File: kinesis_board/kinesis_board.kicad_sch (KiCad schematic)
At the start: 18 parts, among them J2 Conn_01x20, J3 Conn_01x20, J4 Conn_02x03_Odd_Even, J5 Screw_Terminal_01x02, J6 Conn_01x07, U1 ATmega16-16A, U2 D1213A-04S, Y1 Crystal

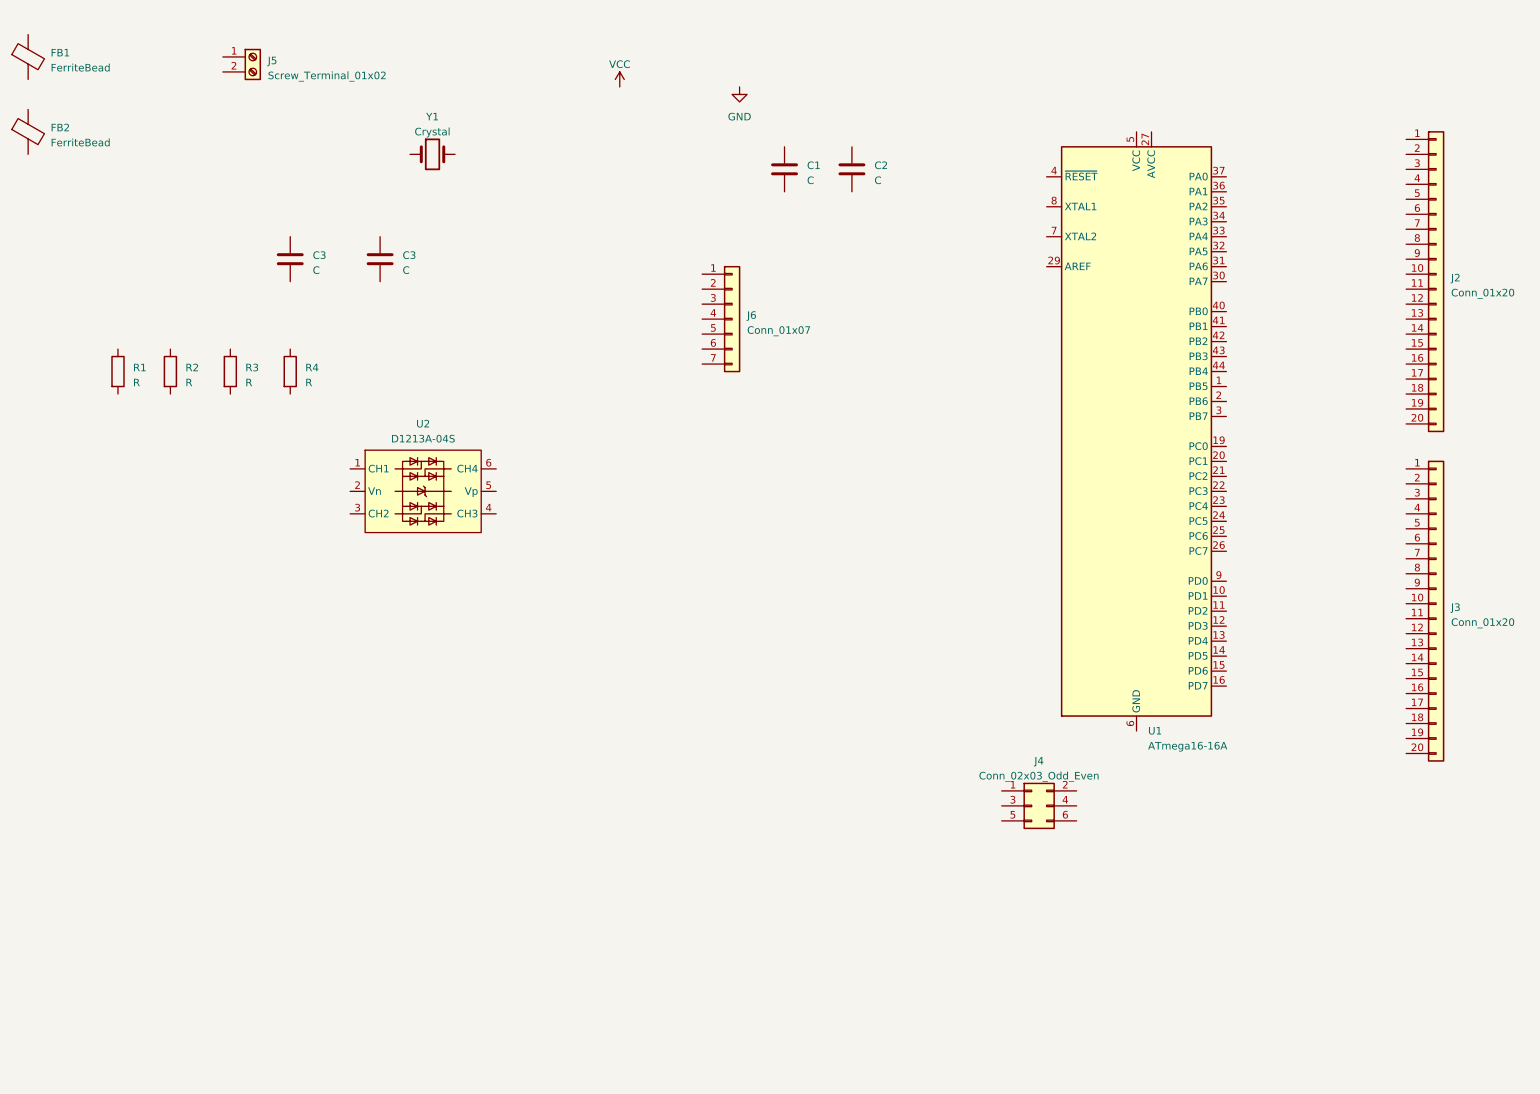
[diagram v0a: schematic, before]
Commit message: finished drawing of the schematics -- needs to be checked before pcb drawing
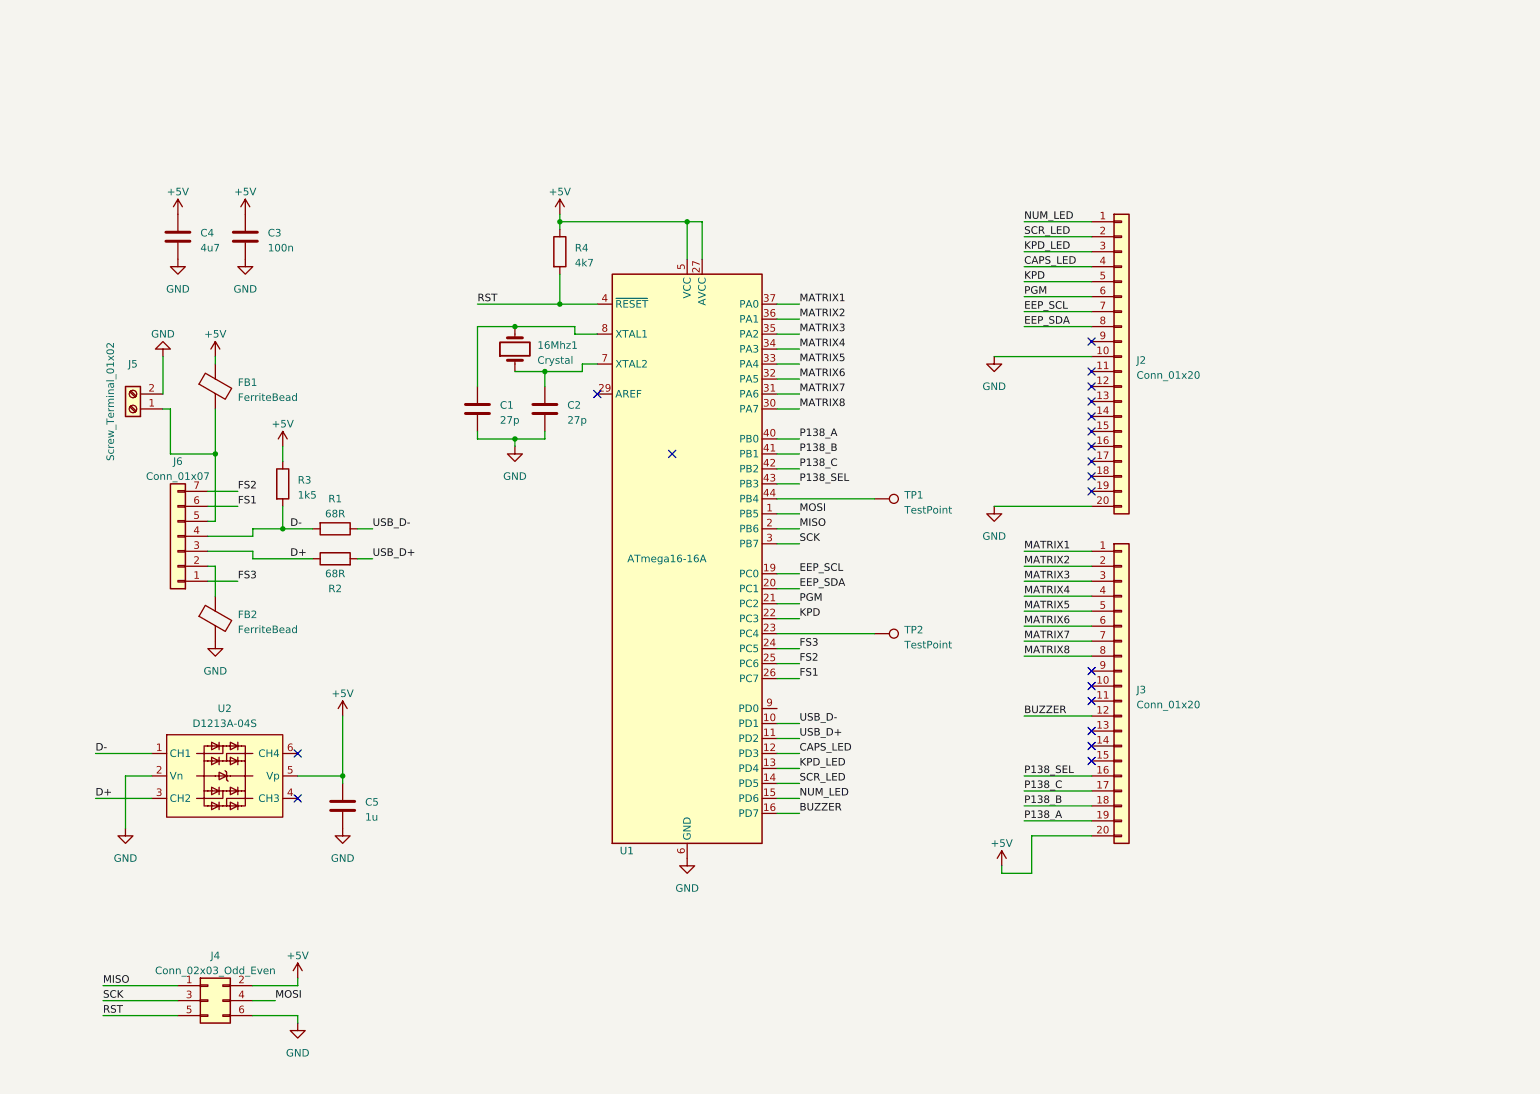
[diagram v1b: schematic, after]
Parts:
- added C5: 1u, Connector_JST:JST_PH_S7B-PH-K_1x07_P2.00mm_Horizontal, symbol Device:C
- added TP1, TP2: TestPoint, TestPoint:TestPoint_Pad_2.0x2.0mm, symbol Connector:TestPoint
- 16Mhz1: renamed from Y1; footprint (none) -> Crystal:Crystal_SMD_HC49-SD_HandSoldering
- C1: value C -> 27p; footprint (none) -> Connector_JST:JST_PH_S7B-PH-K_1x07_P2.00mm_Horizontal
- C2: value C -> 27p; footprint (none) -> Capacitor_SMD:C_0805_2012Metric_Pad1.18x1.45mm_HandSolder
- C3: value C -> 100n; footprint (none) -> Capacitor_SMD:C_0805_2012Metric_Pad1.18x1.45mm_HandSolder
- C4: renamed from C3; value C -> 4u7; footprint (none) -> Capacitor_SMD:C_0805_2012Metric_Pad1.18x1.45mm_HandSolder
- FB1, FB2: footprint (none) -> Inductor_SMD:L_0603_1608Metric_Pad1.05x0.95mm_HandSolder
- J2, J3: footprint (none) -> Connector_PinHeader_2.54mm:PinHeader_1x20_P2.54mm_Vertical_SMD_Pin1Left
- J4: footprint (none) -> Connector_IDC:IDC-Header_2x03_P2.54mm_Horizontal
- J5: footprint (none) -> TerminalBlock_Phoenix:TerminalBlock_Phoenix_MPT-0,5-2-2.54_1x02_P2.54mm_Horizontal
- J6: footprint (none) -> Connector_JST:JST_PH_S7B-PH-K_1x07_P2.00mm_Horizontal
- R1, R2: value R -> 68R; footprint (none) -> Resistor_SMD:R_0805_2012Metric_Pad1.20x1.40mm_HandSolder
- R3: value R -> 1k5; footprint (none) -> Resistor_SMD:R_0805_2012Metric_Pad1.20x1.40mm_HandSolder
- R4: value R -> 4k7; footprint (none) -> Resistor_SMD:R_0805_2012Metric_Pad1.20x1.40mm_HandSolder
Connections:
- net GND: now also C1.2, C2.1, C3.2, C4.2, FB2.2, J2.10 (Pin_10), J2.20 (Pin_20), J4.6 (Pin_6), J5.2 (Pin_2), U1.18 (GND), U1.28 (GND), U1.39 (GND), U1.6 (GND), U2.2 (Vn), C5.2
- net USB_D-: now reaches R1.1
- net USB_D-: now also U1.10 (PD1)
- net D-: now reaches R1.2
- net D-: now also J6.4 (Pin_4), R3.2, U2.1 (CH1)
- net D+: now reaches R2.1
- net D+: now also J6.3 (Pin_3), U2.3 (CH2)
- net USB_D+: now reaches R2.2
- net USB_D+: now also U1.11 (PD2)
- net at J5.1 (Pin_1): now also FB1.2, J6.5 (Pin_5)
- net MATRIX1: now reaches J3.1 (Pin_1)
- net MATRIX1: now also U1.37 (PA0)
- net BUZZER: now reaches J3.12 (Pin_12)
- net BUZZER: now also U1.16 (PD7)
- net P138_SEL: now reaches J3.16 (Pin_16)
- net P138_SEL: now also U1.43 (PB3)
- net P138_C: now reaches J3.17 (Pin_17)
- net P138_C: now also U1.42 (PB2)
- net P138_B: now reaches J3.18 (Pin_18)
- net P138_B: now also U1.41 (PB1)
- net P138_A: now reaches J3.19 (Pin_19)
- net P138_A: now also U1.40 (PB0)
- net MATRIX2: now reaches J3.2 (Pin_2)
- net MATRIX2: now also U1.36 (PA1)
- net +5V: now reaches J3.20 (Pin_20)
- net +5V: now also C3.1, C4.1, FB1.1, J4.2 (Pin_2), R3.1, R4.1, U1.17 (VCC), U1.27 (AVCC), U1.38 (VCC), U1.5 (VCC), U2.5 (Vp), C5.1
- net MATRIX3: now reaches J3.3 (Pin_3)
- net MATRIX3: now also U1.35 (PA2)
- net MATRIX4: now reaches J3.4 (Pin_4)
- net MATRIX4: now also U1.34 (PA3)
- net MATRIX5: now reaches J3.5 (Pin_5)
- net MATRIX5: now also U1.33 (PA4)
- net MATRIX6: now reaches J3.6 (Pin_6)
- net MATRIX6: now also U1.32 (PA5)
- net MATRIX7: now reaches J3.7 (Pin_7)
- net MATRIX7: now also U1.31 (PA6)
- net MATRIX8: now reaches J3.8 (Pin_8)
- net MATRIX8: now also U1.30 (PA7)
- net RST: now reaches R4.2
- net RST: now also J4.5 (Pin_5), U1.4 (~{RESET})
- net at 16Mhz1.1: now also C2.2, U1.7 (XTAL2)
- net at 16Mhz1.2: now also C1.1, U1.8 (XTAL1)
- net FS3: now reaches J6.1 (Pin_1)
- net FS3: now also U1.24 (PC5)
- net at J6.2 (Pin_2): now also FB2.1
- net FS1: now reaches J6.6 (Pin_6)
- net FS1: now also U1.26 (PC7)
- net FS2: now reaches J6.7 (Pin_7)
- net FS2: now also U1.25 (PC6)
- net NUM_LED: now reaches J2.1 (Pin_1)
- net NUM_LED: now also U1.15 (PD6)
- net SCR_LED: now reaches J2.2 (Pin_2)
- net SCR_LED: now also U1.14 (PD5)
- net KPD_LED: now reaches J2.3 (Pin_3)
- net KPD_LED: now also U1.13 (PD4)
- net CAPS_LED: now reaches J2.4 (Pin_4)
- net CAPS_LED: now also U1.12 (PD3)
- net KPD: now reaches J2.5 (Pin_5)
- net KPD: now also U1.22 (PC3)
- net PGM: now reaches J2.6 (Pin_6)
- net PGM: now also U1.21 (PC2)
- net EEP_SCL: now reaches J2.7 (Pin_7)
- net EEP_SCL: now also U1.19 (PC0)
- net EEP_SDA: now reaches J2.8 (Pin_8)
- net EEP_SDA: now also U1.20 (PC1)
- net MISO: now reaches J4.1 (Pin_1)
- net MISO: now also U1.2 (PB6)
- net SCK: now reaches J4.3 (Pin_3)
- net SCK: now also U1.3 (PB7)
- net MOSI: now reaches J4.4 (Pin_4)
- net MOSI: now also U1.1 (PB5)
- net at U1.23 (PC4): now also TP2.1
- net at U1.44 (PB4): now also TP1.1
- no-connect marks 0 -> 20
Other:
- moved on the sheet: 16Mhz1, C1, C2, C3, C4, FB1, FB2, J2, J3, J4, J5, J6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

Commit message: first revision of board - routing needs to be optimized
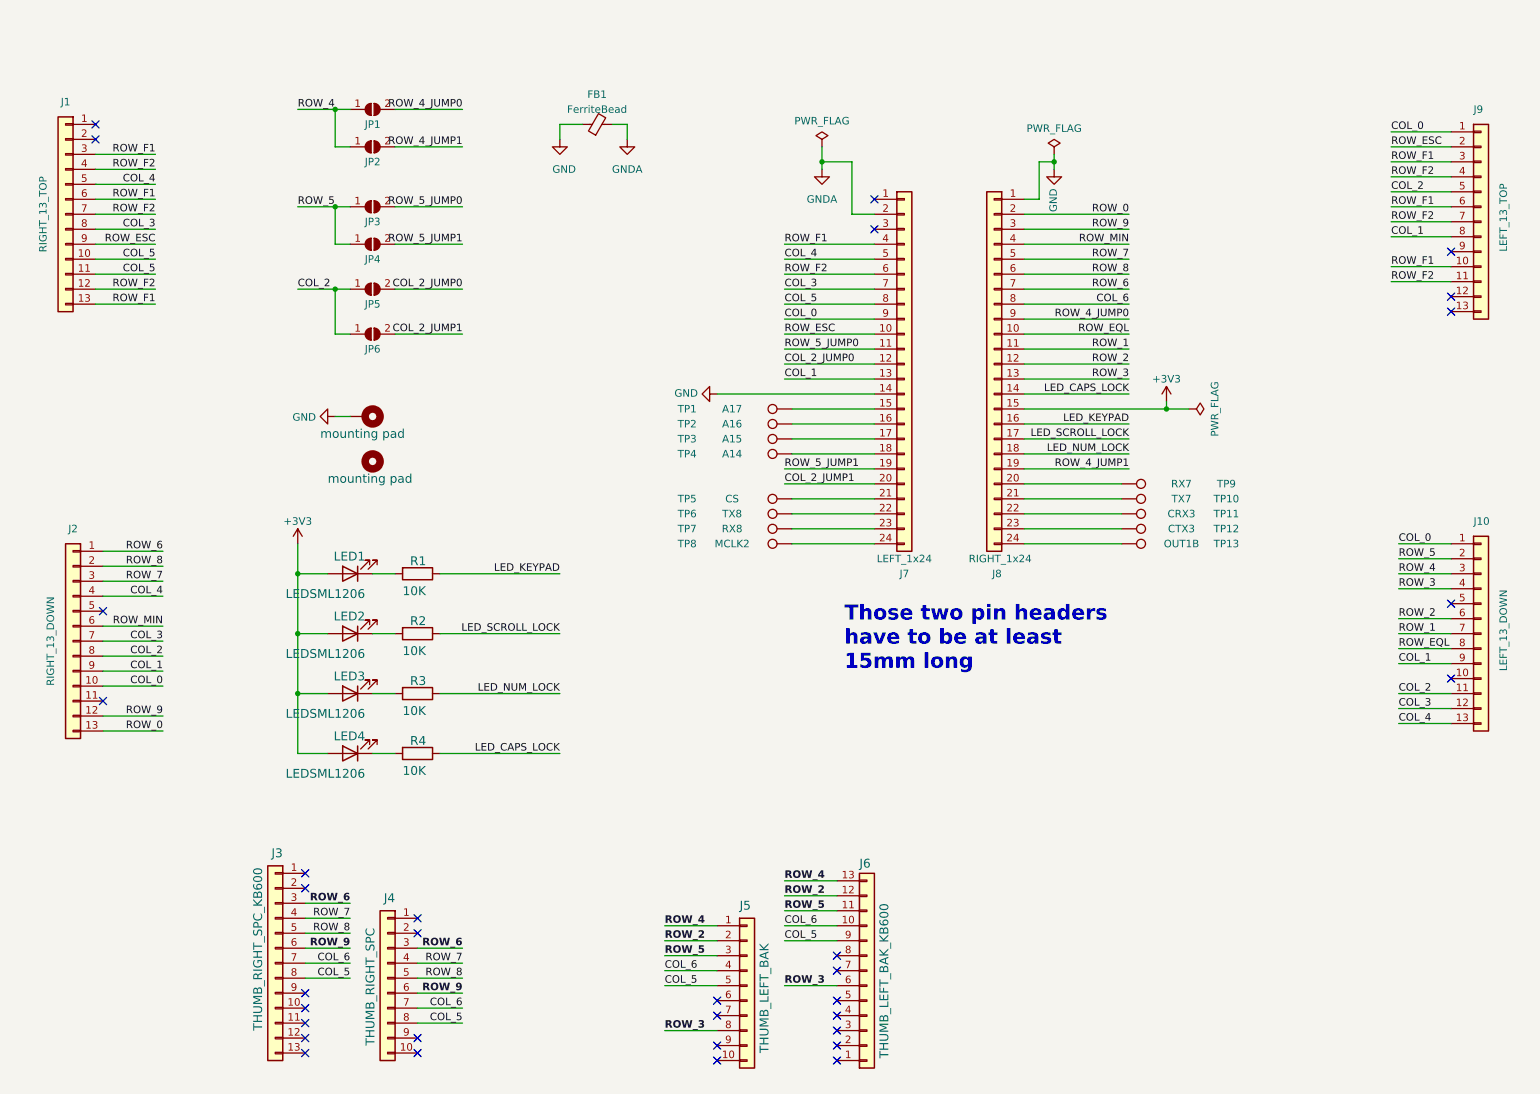
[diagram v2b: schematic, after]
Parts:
- removed 16Mhz1: Crystal, Crystal:Crystal_SMD_HC49-SD_HandSoldering, symbol Device:Crystal
- removed C1: 27p, Connector_JST:JST_PH_S7B-PH-K_1x07_P2.00mm_Horizontal, symbol Device:C
- removed C2: 27p, Capacitor_SMD:C_0805_2012Metric_Pad1.18x1.45mm_HandSolder, symbol Device:C
- removed C3: 100n, Capacitor_SMD:C_0805_2012Metric_Pad1.18x1.45mm_HandSolder, symbol Device:C
- removed C4: 4u7, Capacitor_SMD:C_0805_2012Metric_Pad1.18x1.45mm_HandSolder, symbol Device:C
- removed C5: 1u, Connector_JST:JST_PH_S7B-PH-K_1x07_P2.00mm_Horizontal, symbol Device:C
- removed FB1, FB2: FerriteBead, Inductor_SMD:L_0603_1608Metric_Pad1.05x0.95mm_HandSolder, symbol Device:FerriteBead
- removed J2, J3: Conn_01x20, Connector_PinHeader_2.54mm:PinHeader_1x20_P2.54mm_Vertical_SMD_Pin1Left, symbol Connector_Generic:Conn_01x20
- removed J4: Conn_02x03_Odd_Even, Connector_IDC:IDC-Header_2x03_P2.54mm_Horizontal, symbol Connector_Generic:Conn_02x03_Odd_Even
- removed J5: Screw_Terminal_01x02, TerminalBlock_Phoenix:TerminalBlock_Phoenix_MPT-0,5-2-2.54_1x02_P2.54mm_Horizontal, symbol Connector:Screw_Terminal_01x02
- removed J6: Conn_01x07, Connector_JST:JST_PH_S7B-PH-K_1x07_P2.00mm_Horizontal, symbol Connector_Generic:Conn_01x07
- removed U1: ATmega16-16A, Package_QFP:TQFP-44_10x10mm_P0.8mm, symbol MCU_Microchip_ATmega:ATmega16-16A
- removed U2: D1213A-04S, Package_TO_SOT_SMD:SOT-363_SC-70-6_Handsoldering, symbol dodo_protection:D1213A-04S
- added FB1: FerriteBead, Inductor_SMD:L_0805_2012Metric_Pad1.05x1.20mm_HandSolder, symbol Device:FerriteBead_Small
- added H1: mounting pad, MountingHole:MountingHole_4.3mm_M4_Pad, symbol Mechanical:MountingHole_Pad
- added H2: mounting pad, MountingHole:MountingHole_6mm, symbol Mechanical:MountingHole
- added J1: RIGHT_13_TOP, dodo_conn:Molex-39-53-2135, symbol Connector_Generic:Conn_01x13
- added J10: LEFT_13_DOWN, dodo_conn:Molex-39-53-2135, symbol Connector_Generic:Conn_01x13
- added J2: RIGHT_13_DOWN, dodo_conn:Molex-39-53-2135, symbol Connector_Generic:Conn_01x13
- added J3: THUMB_RIGHT_SPC_KB600, dodo_conn:Molex-39-53-2135, symbol Connector_Generic:Conn_01x13
- added J4: THUMB_RIGHT_SPC, Connector_PinHeader_2.54mm:PinHeader_1x10_P2.54mm_Vertical, symbol Connector_Generic:Conn_01x10
- added J5: THUMB_LEFT_BAK, Connector_PinHeader_2.54mm:PinHeader_1x10_P2.54mm_Vertical, symbol Connector_Generic:Conn_01x10
- added J6: THUMB_LEFT_BAK_KB600, dodo_conn:Molex-39-53-2135, symbol Connector_Generic:Conn_01x13
- added J7: LEFT_1x24, Connector_PinHeader_2.54mm:PinHeader_1x24_P2.54mm_Vertical, symbol Connector_Generic:Conn_01x24
- added J8: RIGHT_1x24, Connector_PinHeader_2.54mm:PinHeader_1x24_P2.54mm_Vertical, symbol Connector_Generic:Conn_01x24
- added J9: LEFT_13_TOP, dodo_conn:Molex-39-53-2135, symbol Connector_Generic:Conn_01x13
- added JP1, JP2, JP3, JP4, JP5, JP6: SolderJumper_2_Open, Jumper:SolderJumper-2_P1.3mm_Open_RoundedPad1.0x1.5mm, symbol Jumper:SolderJumper_2_Open
- added LED1, LED2, LED3, LED4: LEDSML1206, LED_SMD:LED_1206_3216Metric_Pad1.42x1.75mm_HandSolder, symbol Device:LED
- added TP10: TX7, TestPoint:TestPoint_Pad_D2.0mm, symbol Connector:TestPoint
- added TP11: CRX3, TestPoint:TestPoint_Pad_D2.0mm, symbol Connector:TestPoint
- added TP12: CTX3, TestPoint:TestPoint_Pad_D2.0mm, symbol Connector:TestPoint
- added TP13: OUT1B, TestPoint:TestPoint_Pad_D2.0mm, symbol Connector:TestPoint
- added TP3: A15, TestPoint:TestPoint_Pad_D2.0mm, symbol Connector:TestPoint
- added TP4: A14, TestPoint:TestPoint_Pad_D2.0mm, symbol Connector:TestPoint
- added TP5: CS, TestPoint:TestPoint_Pad_D2.0mm, symbol Connector:TestPoint
- added TP6: TX8, TestPoint:TestPoint_Pad_D2.0mm, symbol Connector:TestPoint
- added TP7: RX8, TestPoint:TestPoint_Pad_D2.0mm, symbol Connector:TestPoint
- added TP8: MCLK2, TestPoint:TestPoint_Pad_D2.0mm, symbol Connector:TestPoint
- added TP9: RX7, TestPoint:TestPoint_Pad_D2.0mm, symbol Connector:TestPoint
- R1, R2: value 68R -> 10K; MPN (none) -> CRCW120610K0FKEAC; digikeypn (none) -> 541-3983-1-ND; mouserpn (none) -> 71-CRCW120610K0FKEAC
- R3: value 1k5 -> 10K; MPN (none) -> CRCW120610K0FKEAC; digikeypn (none) -> 541-3983-1-ND; mouserpn (none) -> 71-CRCW120610K0FKEAC
- R4: value 4k7 -> 10K; MPN (none) -> CRCW120610K0FKEAC; digikeypn (none) -> 541-3983-1-ND; mouserpn (none) -> 71-CRCW120610K0FKEAC
- TP1: value TestPoint -> A17; footprint TestPoint:TestPoint_Pad_2.0x2.0mm -> TestPoint:TestPoint_Pad_D2.0mm
- TP2: value TestPoint -> A16; footprint TestPoint:TestPoint_Pad_2.0x2.0mm -> TestPoint:TestPoint_Pad_D2.0mm
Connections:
- net GND: now also FB1.1, H1.1, J7.14 (Pin_14), J8.1 (Pin_1)
- net at TP2.1: now also J7.16 (Pin_16)
- net at TP1.1: now also J7.15 (Pin_15)
- net +5V renamed LED_CAPS_LOCK
- net LED_CAPS_LOCK: now also J8.14 (Pin_14); no longer R3.1
- net D+ renamed LED_SCROLL_LOCK
- net LED_SCROLL_LOCK: now also J8.17 (Pin_17)
- net D-: no longer names the net of R1.2
- net D-: now also LED1.1 (K); no longer R3.2
- net RST: no longer names the net of R4.2
- net RST: now also LED4.1 (K)
- net USB_D+: no longer names the net of R2.2
- net USB_D+: now also LED2.1 (K)
- net USB_D- renamed LED_KEYPAD
- net LED_KEYPAD: now also J8.16 (Pin_16)
- new net: J8.21 (Pin_21), TP10.1
- new net: J7.18 (Pin_18), TP4.1
- new net: J7.17 (Pin_17), TP3.1
- new net: J7.21 (Pin_21), TP5.1
- new net: J7.22 (Pin_22), TP6.1
- new net: J7.23 (Pin_23), TP7.1
- new net: J7.24 (Pin_24), TP8.1
- new net: J8.20 (Pin_20), TP9.1
- new net: J8.24 (Pin_24), TP13.1
- new net: J8.22 (Pin_22), TP11.1
- new net: J8.23 (Pin_23), TP12.1
- new net: LED3.1 (K), R3.2
- new net +3V3: J8.15 (Pin_15), LED1.2 (A), LED2.2 (A), LED3.2 (A), LED4.2 (A)
- new net COL_0: J10.1 (Pin_1), J2.10 (Pin_10), J7.9 (Pin_9), J9.1 (Pin_1)
- new net COL_1: J10.9 (Pin_9), J2.9 (Pin_9), J7.13 (Pin_13), J9.8 (Pin_8)
- new net COL_2: J10.11 (Pin_11), J2.8 (Pin_8), J9.5 (Pin_5), JP5.1 (A), JP6.1 (A)
- new net COL_2_JUMP0: J7.12 (Pin_12), JP5.2 (B)
- new net COL_2_JUMP1: J7.20 (Pin_20), JP6.2 (B)
- new net COL_3: J1.8 (Pin_8), J10.12 (Pin_12), J2.7 (Pin_7), J7.7 (Pin_7)
- new net COL_4: J1.5 (Pin_5), J10.13 (Pin_13), J2.4 (Pin_4), J7.5 (Pin_5)
- new net COL_5: J1.10 (Pin_10), J1.11 (Pin_11), J3.8 (Pin_8), J4.8 (Pin_8), J5.5 (Pin_5), J6.9 (Pin_9), J7.8 (Pin_8)
- new net COL_6: J3.7 (Pin_7), J4.7 (Pin_7), J5.4 (Pin_4), J6.10 (Pin_10), J8.8 (Pin_8)
- new net GNDA: FB1.2, J7.2 (Pin_2)
- new net LED_NUM_LOCK: J8.18 (Pin_18), R3.1
- new net ROW_0: J2.13 (Pin_13), J8.2 (Pin_2)
- new net ROW_1: J10.7 (Pin_7), J8.11 (Pin_11)
- new net ROW_2: J10.6 (Pin_6), J5.2 (Pin_2), J6.12 (Pin_12), J8.12 (Pin_12)
- new net ROW_3: J10.4 (Pin_4), J5.8 (Pin_8), J6.6 (Pin_6), J8.13 (Pin_13)
- new net ROW_4: J10.3 (Pin_3), J5.1 (Pin_1), J6.13 (Pin_13), JP1.1 (A), JP2.1 (A)
- new net ROW_4_JUMP0: J8.9 (Pin_9), JP1.2 (B)
- new net ROW_4_JUMP1: J8.19 (Pin_19), JP2.2 (B)
- new net ROW_5: J10.2 (Pin_2), J5.3 (Pin_3), J6.11 (Pin_11), JP3.1 (A), JP4.1 (A)
- new net ROW_5_JUMP0: J7.11 (Pin_11), JP3.2 (B)
- new net ROW_5_JUMP1: J7.19 (Pin_19), JP4.2 (B)
- new net ROW_6: J2.1 (Pin_1), J3.3 (Pin_3), J4.3 (Pin_3), J8.7 (Pin_7)
- new net ROW_7: J2.3 (Pin_3), J3.4 (Pin_4), J4.4 (Pin_4), J8.5 (Pin_5)
- new net ROW_8: J2.2 (Pin_2), J3.5 (Pin_5), J4.5 (Pin_5), J8.6 (Pin_6)
- new net ROW_9: J2.12 (Pin_12), J3.6 (Pin_6), J4.6 (Pin_6), J8.3 (Pin_3)
- new net ROW_EQL: J10.8 (Pin_8), J8.10 (Pin_10)
- new net ROW_ESC: J1.9 (Pin_9), J7.10 (Pin_10), J9.2 (Pin_2)
- new net ROW_F1: J1.13 (Pin_13), J1.3 (Pin_3), J1.6 (Pin_6), J7.4 (Pin_4), J9.10 (Pin_10), J9.3 (Pin_3), J9.6 (Pin_6)
- new net ROW_F2: J1.12 (Pin_12), J1.4 (Pin_4), J1.7 (Pin_7), J7.6 (Pin_6), J9.11 (Pin_11), J9.4 (Pin_4), J9.7 (Pin_7)
- new net ROW_MIN: J2.6 (Pin_6), J8.4 (Pin_4)
- no-connect marks 20 -> 33
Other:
- note added: "Those two pin headers have to be at least 15mm long"
- title: (none) -> QMK BOARD FOR KINESIS ADVANTAGE
